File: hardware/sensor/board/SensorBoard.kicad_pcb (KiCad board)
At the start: 4 copper layers, 40 x 25 mm, 44 parts, among them J1 USB_B_Mini, J2 Conn_01x04_Male, U1 93LC56BT-I/OT, U2 FT232H, U3 74LVC2G17, U4 74LVC1G374, U5 74LVC1G04, Y1 12MHz

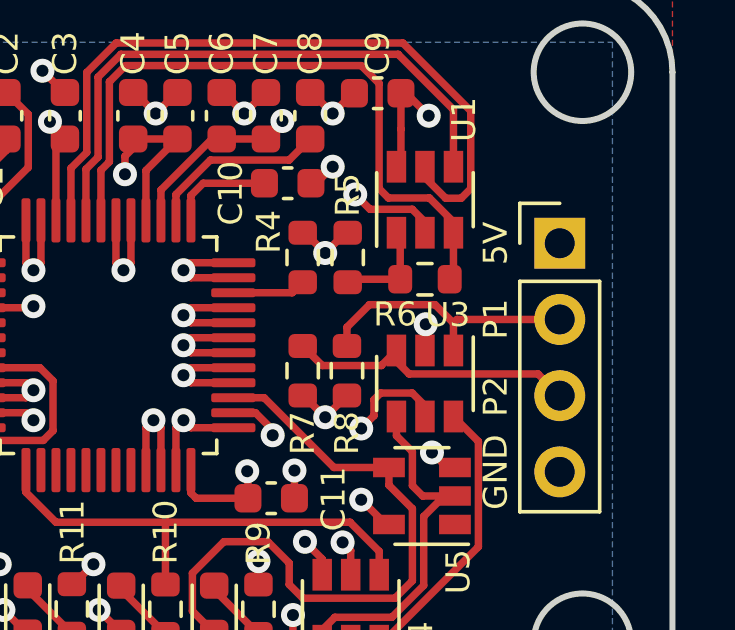
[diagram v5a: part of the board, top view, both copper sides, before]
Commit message: Replacing decoder Schmitt IC
Replacing LVC2G17 (Dual Schmitt Trigger Input Buffers) with LVC2G14 (Dual Schmitt Inverter)
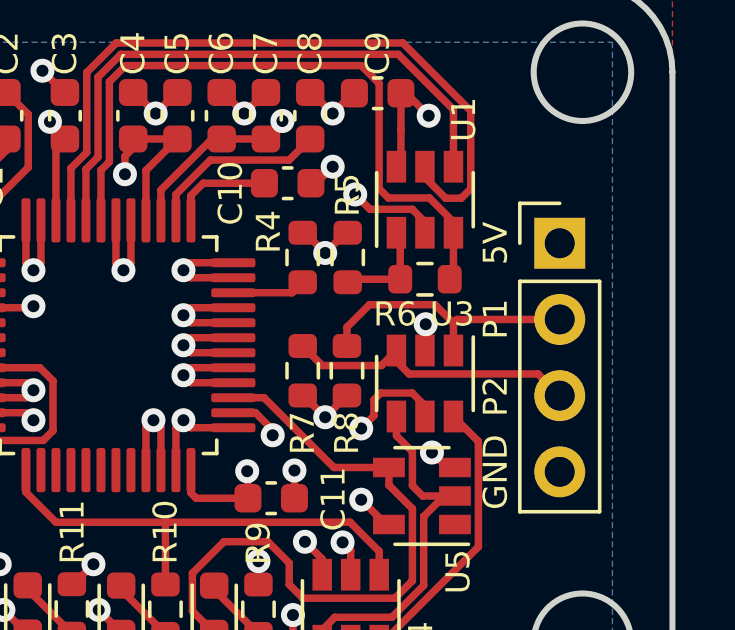
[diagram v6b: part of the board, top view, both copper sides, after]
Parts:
- C1, C2: value 27pF -> 8pF
- U3: value 74LVC2G17 -> 74LVC2G14

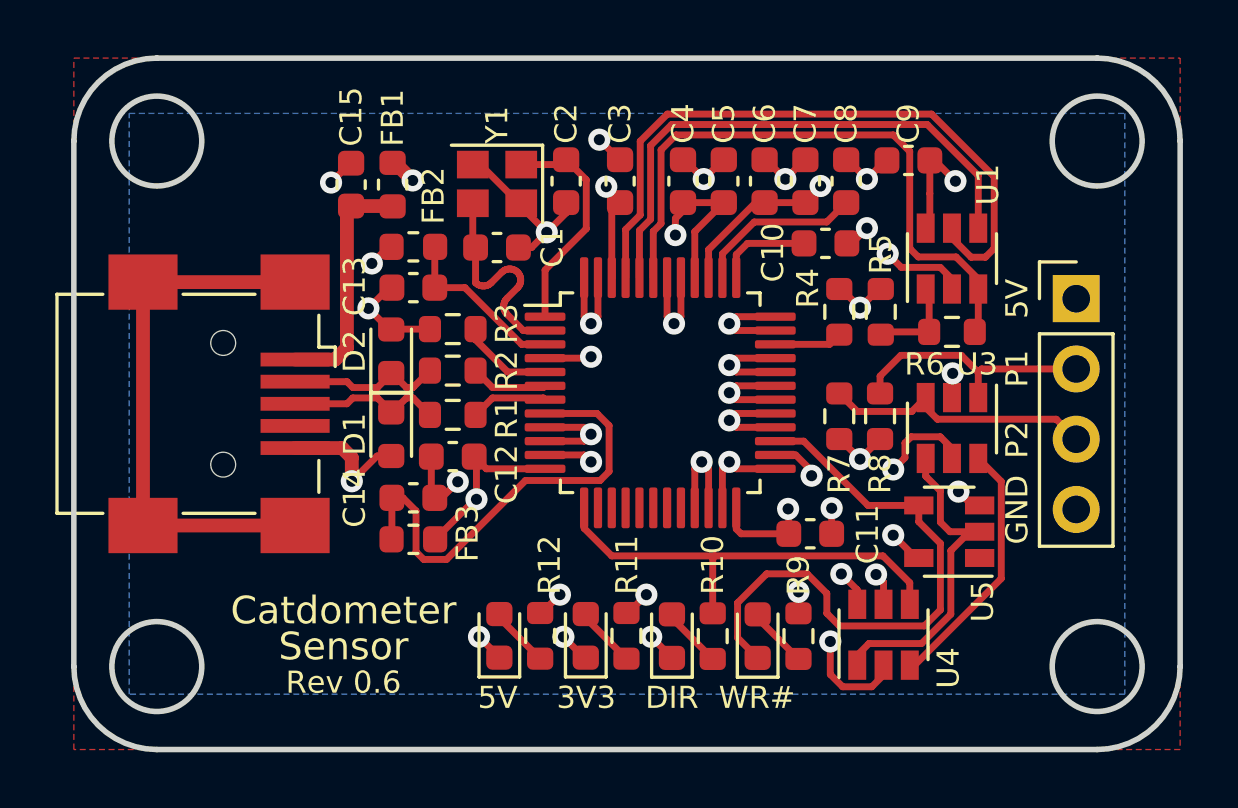
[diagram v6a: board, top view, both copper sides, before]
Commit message: Updating to KiCad 6.0
Updating schematic to KiCad 6.0, cleaning up some cache files.
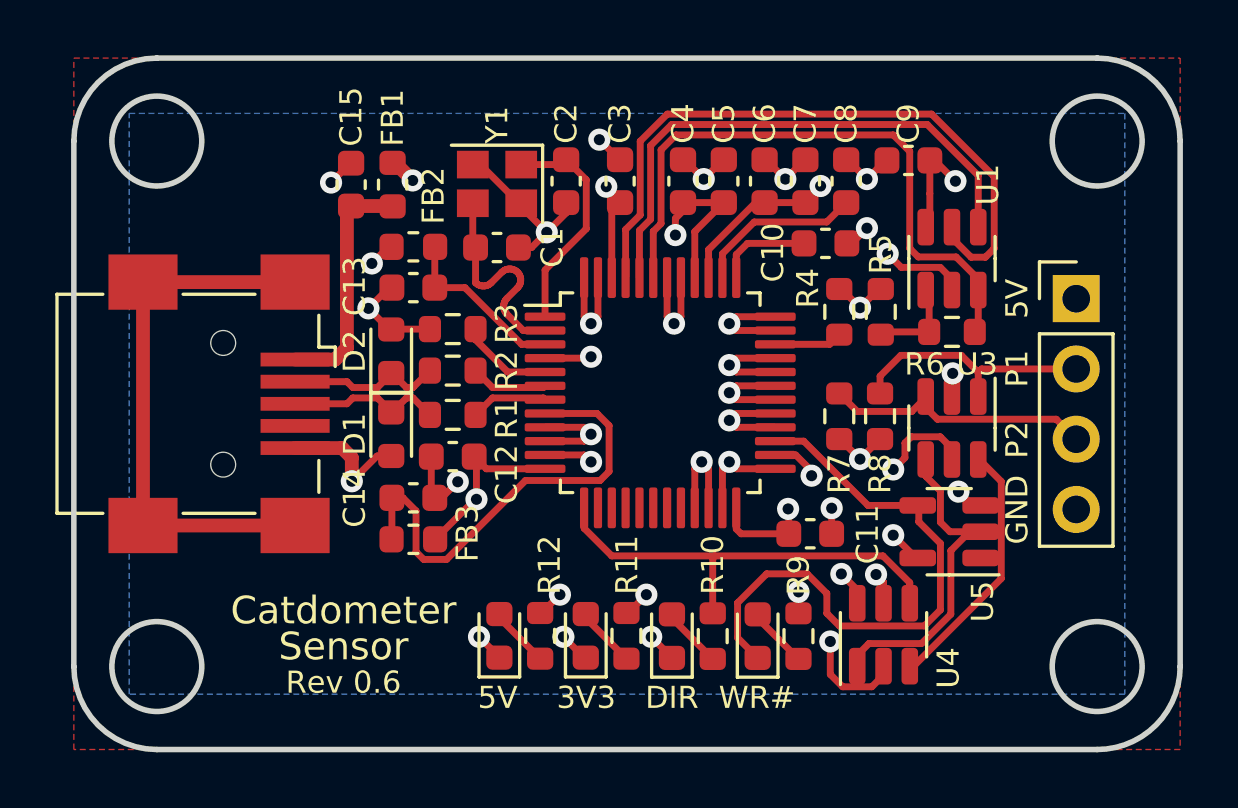
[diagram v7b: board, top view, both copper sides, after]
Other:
- net class Default removed
